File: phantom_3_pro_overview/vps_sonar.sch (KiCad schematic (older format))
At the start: 0 parts

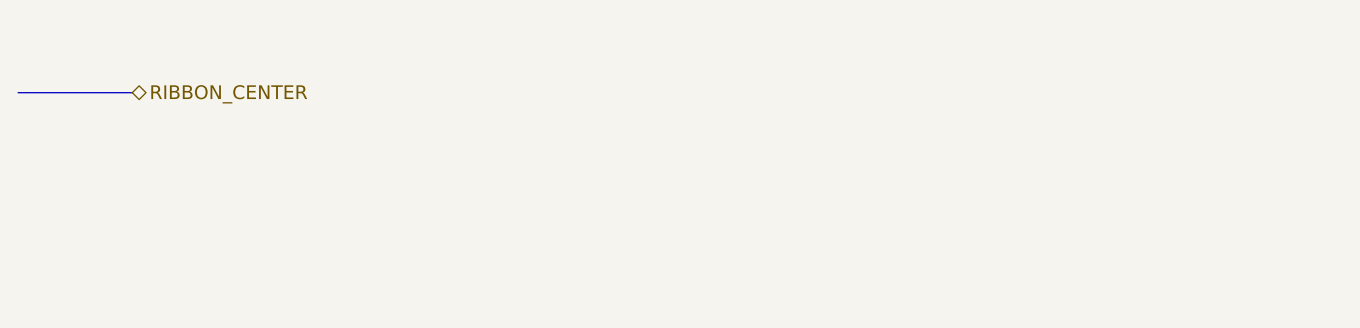
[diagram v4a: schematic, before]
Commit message: Overview: Updated VPS definition.
Placed proper components into VPS schematics.
No connections are made between components yet.
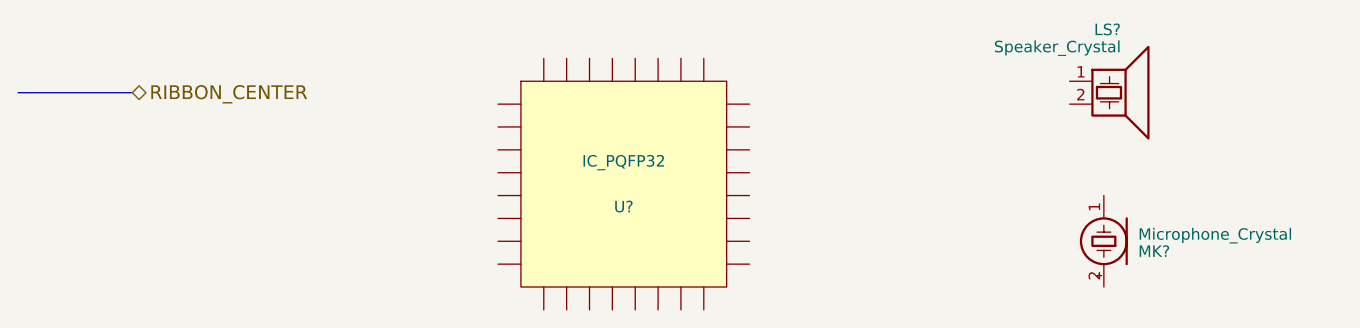
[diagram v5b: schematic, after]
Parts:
- added LS?: Speaker_Crystal, symbol Speaker_Crystal
- added MK?: Microphone_Crystal, symbol Microphone_Crystal
- added U?: IC_PQFP32, MODULE, symbol IC_PQFP32
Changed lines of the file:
@@
 Text HLabel 2800 2050 2    60   BiDi ~ 0
 RIBBON_CENTER
+$Comp
+L IC_PQFP32 U?
+U 1 1 597EF5D6
+P 4950 2450
+F 0 "U?" H 4950 2350 50  0000 C CNN
+F 1 "IC_PQFP32" H 4950 2550 50  0000 C CNN
+F 2 "MODULE" H 4950 2450 50  0001 C CNN
+F 3 "DOCUMENTATION" H 4950 2450 50  0001 C CNN
+	1    4950 2450
+	1    0    0    -1
+$EndComp
+$Comp
+L Speaker_Crystal LS?
+U 1 1 597EF639
+P 7100 2000
+F 0 "LS?" H 7125 2225 50  0000 R CNN
+F 1 "Speaker_Crystal" H 7125 2150 50  0000 R CNN
+F 2 "" H 7065 1950 50  0001 C CNN
+F 3 "" H 7065 1950 50  0001 C CNN
+	1    7100 2000
+	1    0    0    -1
+$EndComp
+$Comp
+L Microphone_Crystal MK?
+U 1 1 597EF688
+P 7050 2700
+F 0 "MK?" H 6900 2745 50  0000 R CNN
+F 1 "Microphone_Crystal" H 6900 2670 50  0000 R CNN
+F 2 "" V 7100 2630 50  0001 L CNN
+F 3 "" V 7050 2800 50  0001 C CNN
+	1    7050 2700
+	-1   0    0    1
+$EndComp
 $EndSCHEMATC

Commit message: Overview: Upgraded to KiCAD 5.0.1.
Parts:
- LS?: symbol Speaker_Crystal -> Device:Speaker_Crystal
- MK?: symbol Microphone_Crystal -> Device:Microphone_Crystal
- U?: symbol IC_PQFP32 -> ic_dil_generic:IC_PQFP32
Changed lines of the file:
@@
-EESchema Schematic File Version 2
-LIBS:power
-LIBS:device
-LIBS:transistors
-LIBS:conn
-LIBS:linear
-LIBS:regul
-LIBS:74xx
-LIBS:cmos4000
-LIBS:adc-dac
-LIBS:memory
-LIBS:xilinx
-LIBS:microcontrollers
-LIBS:dsp
-LIBS:microchip
-LIBS:analog_switches
-LIBS:motorola
-LIBS:texas
-LIBS:intel
-LIBS:audio
-LIBS:interface
-LIBS:digital-audio
-LIBS:philips
-LIBS:display
-LIBS:cypress
-LIBS:siliconi
-LIBS:opto
-LIBS:atmel
-LIBS:contrib
-LIBS:valves
-LIBS:motors
-LIBS:ic_dil_generic
-LIBS:sensors
-LIBS:u-blox
-LIBS:amplifiers
-LIBS:transistors-switches
-LIBS:transistors-power
-LIBS:sensors-v2
-LIBS:regul-v2
+EESchema Schematic File Version 4
 LIBS:phantom_3_pro_overview-cache
-EELAYER 25 0
+EELAYER 26 0
 EELAYER END
 $Descr A4 11693 8268
@@
 RIBBON_CENTER
 $Comp
-L IC_PQFP32 U?
+L ic_dil_generic:IC_PQFP32 U?
 U 1 1 597EF5D6
 P 4950 2450
@@
 $EndComp
 $Comp
-L Speaker_Crystal LS?
+L Device:Speaker_Crystal LS?
 U 1 1 597EF639
 P 7100 2000
@@
 $EndComp
 $Comp
-L Microphone_Crystal MK?
+L Device:Microphone_Crystal MK?
 U 1 1 597EF688
 P 7050 2700
